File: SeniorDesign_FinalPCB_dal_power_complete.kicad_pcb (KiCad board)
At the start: 2 copper layers, 172.7 x 167.4 mm, 262 parts, among them J1 5000, J10 5000, J11 POWER, J12 AudioJack3, J2 5000, J3 5000, J4 5000, J5 5000, J6 5000, J7 5000, J8 5000, J9 5000, Q1 Si7450DP, Q10 Si7450DP, Q11 Si7450DP, Q12 Si7450DP, Q13 Si7450DP, Q14 Si7450DP, Q15 Si7450DP, Q16 Si7450DP, Q2 Si7450DP, Q3 Si7450DP, Q4 Si7450DP, Q5 Si7450DP, Q6 Si7450DP, Q7 Si7450DP, Q8 Si7450DP, Q9 Si7450DP, U1 Transducer, U10 Transducer, U11 Transducer, U12 Transducer, U13 Transducer, U14 Transducer, U15 Transducer, U16 Transducer, U17 Transducer, U18 Transducer, U19 Transducer, U2 Transducer, U20 Transducer, U21 Transducer, U22 Transducer, U23 Transducer, U24 Transducer, U25 Transducer, U26 Transducer, U27 Transducer, U28 Transducer, U29 Transducer, U3 Transducer, U30 Transducer, U31 Transducer, U32 Transducer, U33 Transducer, U34 Transducer, U35 Transducer, U36 Transducer, U37 Transducer, U38 Transducer, U39 Transducer, U4 Transducer, U40 Transducer, U41 Transducer, U42 Transducer, U43 Transducer, U44 Transducer, U45 Transducer, U46 Transducer, U47 Transducer, U48 Transducer, U49 Transducer, U5 Transducer, U50 Transducer, U51 Transducer, U52 Transducer, U53 Transducer, U54 Transducer, U55 Transducer, U56 Transducer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

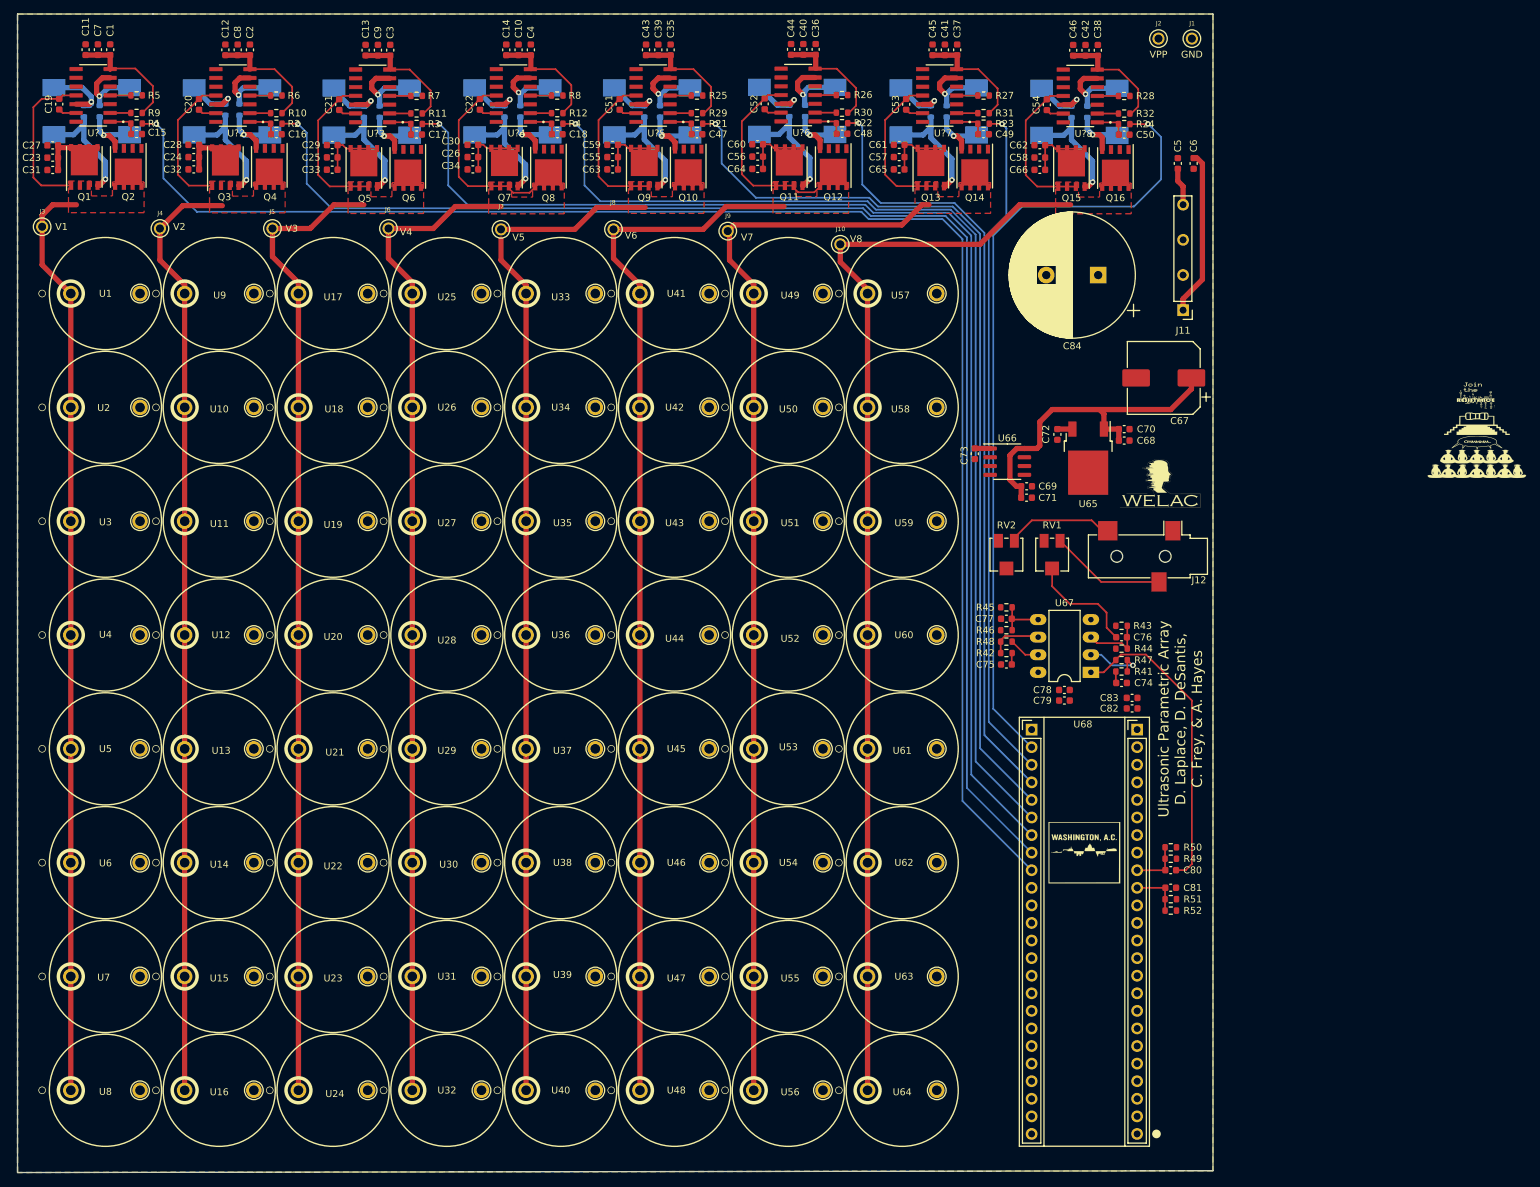
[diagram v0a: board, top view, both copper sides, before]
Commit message: Replaced 0603 Caps (VPP) with 1206
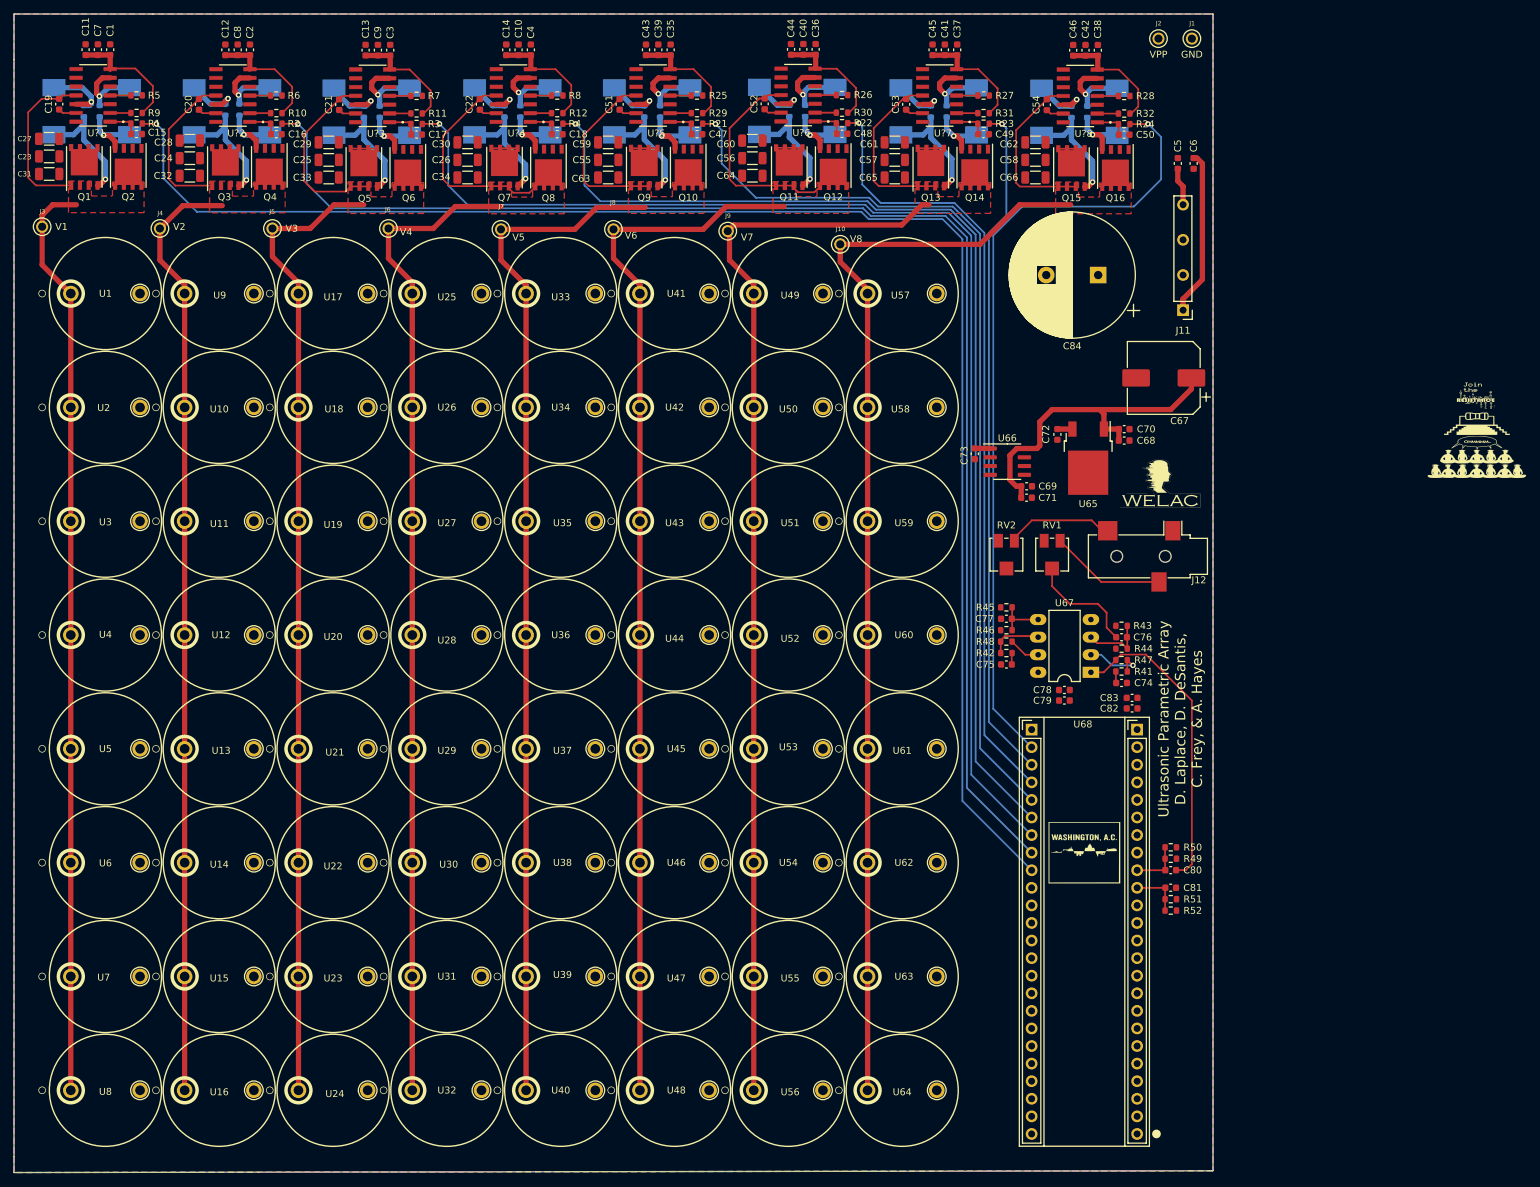
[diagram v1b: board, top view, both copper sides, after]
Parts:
- C23, C24, C25, C26, C27, C28, C29, C30, C31, C32, C33, C34, C55, C56, C57, C58, C59, C60, C61, C62, C63, C64, C65, C66: footprint Capacitor_SMD:C_0603_1608Metric -> SeniorDesign:C_1206_3216Metric
- moved C34 1.40 mm to (367.3, 43.4)
- moved C65 1.33 mm to (429.0, 43.4)
- moved C63 1.33 mm to (387.6, 43.4)
- moved C66 1.28 mm to (449.3, 43.4)
- moved C64 1.25 mm to (408.4, 43.2)
- moved C33 1.24 mm to (347.2, 43.4)
- moved C32 1.08 mm to (327.2, 43.2)
- moved C27 1.07 mm to (306.8, 37.8)
- moved C60 0.93 mm to (408.4, 38.1)
- moved C26 0.87 mm to (367.3, 40.9)
- moved C30 0.84 mm to (367.3, 38.4)
- moved C28 0.83 mm to (327.2, 38.1)
- moved C56 0.79 mm to (408.4, 40.6)
- moved C31 0.77 mm to (306.8, 42.9)
- moved C62 0.76 mm to (449.3, 38.4)
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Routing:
- net VPP: track 81.1 -> 28.4 mm
- net COL5_OUT: track 169.9 -> 174.8 mm
- net COL3_OUT: track 163.8 -> 167.8 mm
- net COL4_OUT: track 170.5 -> 174.0 mm
- net COL6_OUT: track 178.9 -> 182.3 mm
- net COL7_OUT: track 178.5 -> 181.6 mm
- net COL8_OUT: track 182.7 -> 185.3 mm
- net COL2_OUT: track 157.2 -> 159.4 mm
- net COL1_OUT: track 156.7 -> 157.8 mm
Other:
- board size 172.7 x 167.4 mm -> 173.2 x 167.4 mm

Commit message: Routing the rest of the things. (Subject to change)
This is my attempt at routing all of the rest of the things. I used (Pcbnew / Tools / Cleanup Tracks & Via’s) to remove all of the small "unconnected track" warnings we were getting and in this configuration I now get 14 errors, but the DRC completes.
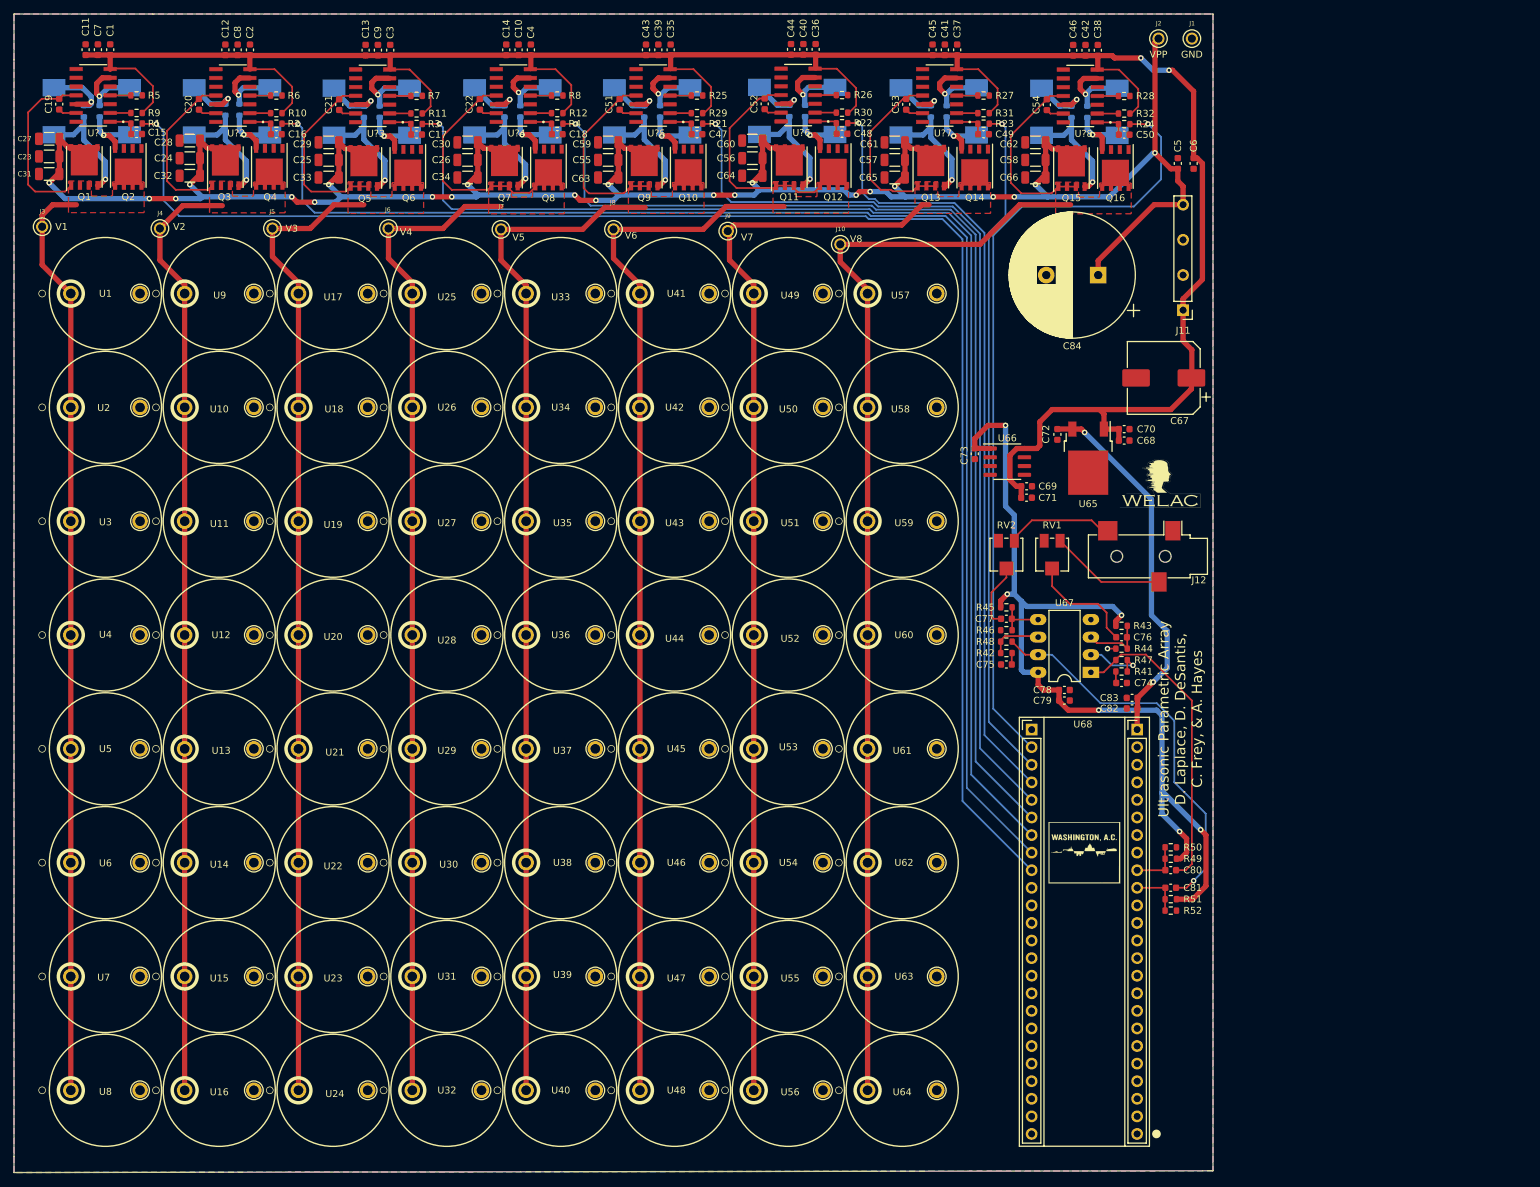
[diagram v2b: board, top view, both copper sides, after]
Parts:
- G*** (x2): moved to B.Cu
- moved G*** 62.2 mm to (452.2, 70.1), turned to 180 degrees
- moved G*** 56.2 mm to (455.2, 65.0), turned to 180 degrees
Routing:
- net VPP: track 28.4 -> 330.0 mm, vias 0 -> 23
- net +12V: track 207.6 -> 361.5 mm, vias 0 -> 2
- net +5VA: track 2.23 -> 135.1 mm, vias 0 -> 6
- net Net-(C81-Pad1): track 4.55 -> 56.8 mm, vias 0 -> 1
- net +5V: track 2.17 -> 53.8 mm, vias 0 -> 2
- net Net-(C77-Pad1): track 0.00 -> 9.40 mm
- net COL5_SIG: track 134.4 -> 136.8 mm
- net Net-(D2-Pad2): track 12.0 -> 9.71 mm
- net Net-(D5-Pad2): track 18.6 -> 16.7 mm
- net COL8_OUT: track 185.3 -> 187.2 mm
- net COL1_SIG: track 224.8 -> 226.6 mm
- net COL2_SIG: track 202.8 -> 204.6 mm
- net COL3_SIG: track 180.7 -> 182.4 mm
- net COL5_OUT: track 174.8 -> 176.2 mm
- net COL1_OUT: track 157.8 -> 159.1 mm
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
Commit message: final pre-design review push
Fixed some routing problems. Changed capacitor sizes for large bypass voltages. array modeled
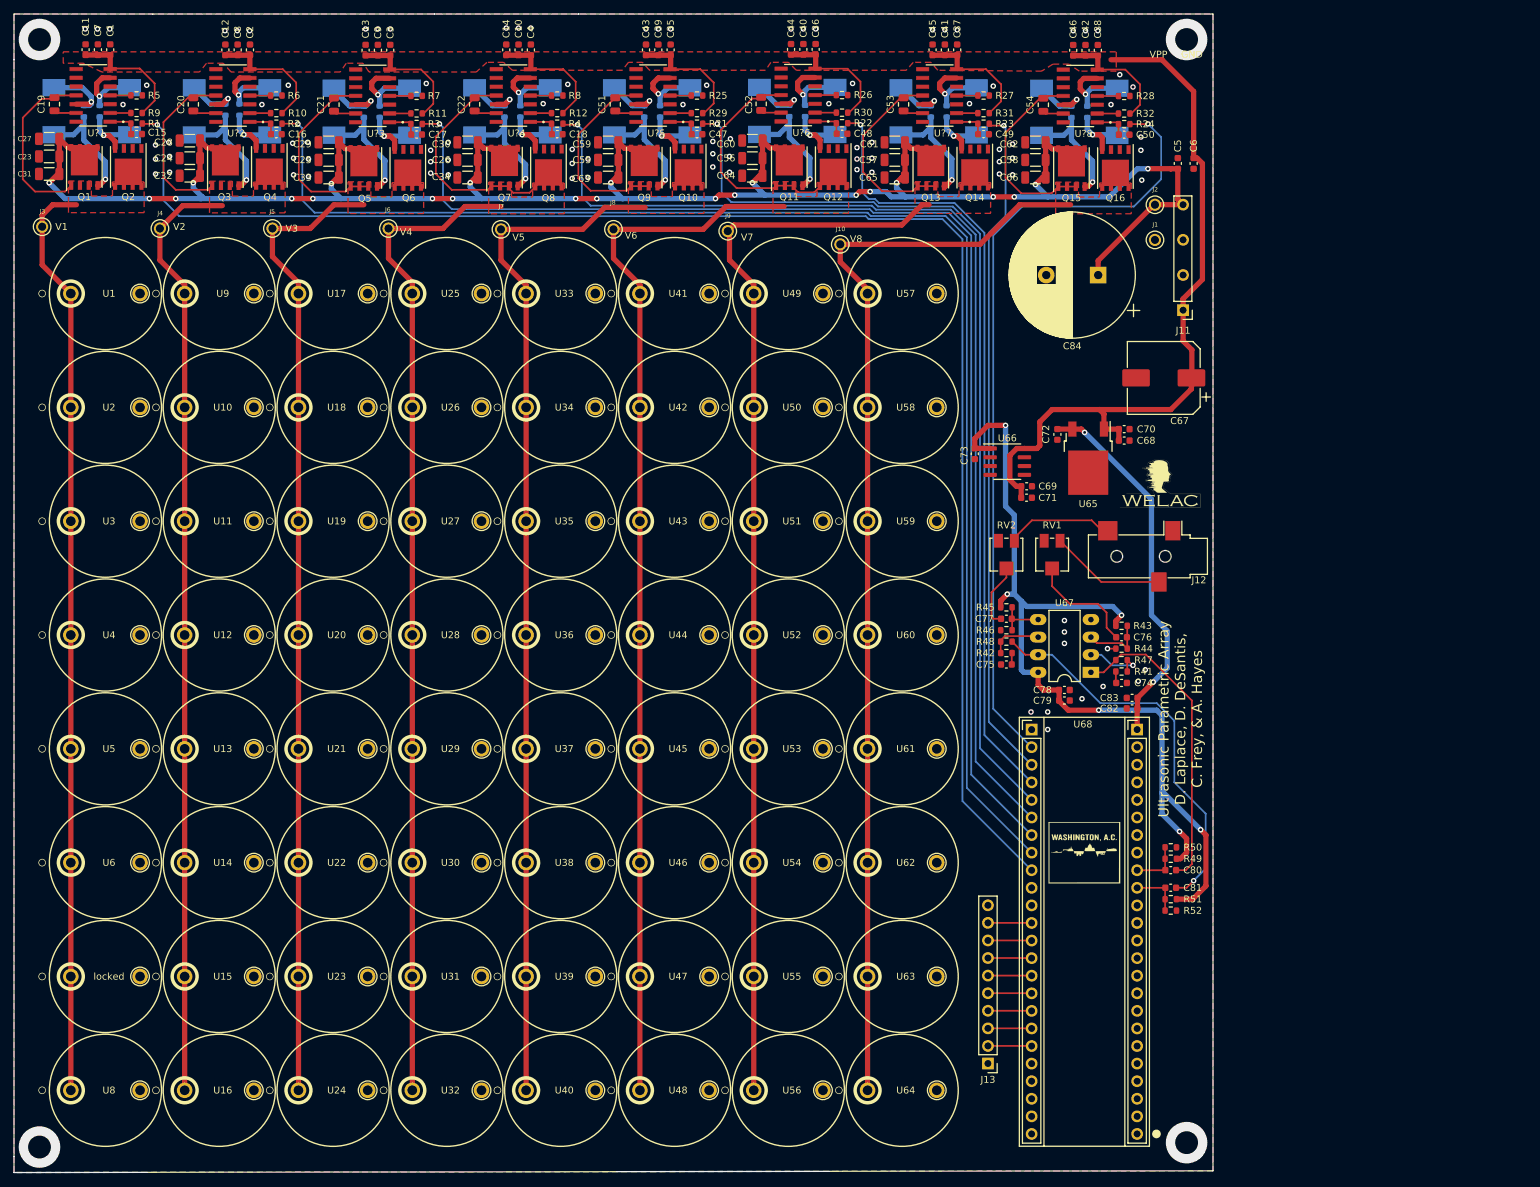
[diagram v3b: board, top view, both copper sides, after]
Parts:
- added J13: Conn_01x10_Male, Connector_PinHeader_2.54mm:PinHeader_1x10_P2.54mm_Vertical, F.Cu at (442.5, 171.4)
- C19, C20, C21, C22, C51, C52, C53, C54: value 0.1u -> 0.1u 100V; footprint Capacitor_SMD:C_0603_1608Metric -> Capacitor_SMD:C_0805_2012Metric
- C27, C29, C30, C59, C60, C61, C62: value 0.1u -> 0.1u 100V
- C28: value 1u -> 0.1u 100V
- C31, C32, C33, C34, C63, C64, C65, C66: value 0.1u -> 100p 100V
- U1, U10, U11, U12, U13, U14, U15, U16, U17, U18, U19, U2, U20, U21, U22, U23, U24, U25, U26, U27, U28, U29, U3, U30, U31, U32, U33, U34, U35, U36, U37, U38, U39, U4, U40, U41, U42, U43, U44, U45, U46, U47, U48, U49, U5, U50, U51, U52, U53, U54, U55, U56, U57, U58, U59, U6, U60, U61, U62, U63, U64, U8, U9: footprint SeniorDesign:Transducer -> Senior:Transducer
- locked: renamed from U7; footprint SeniorDesign:Transducer -> Senior:Transducer
- moved J1 29.6 mm to (466.6, 52.5)
- moved J2 24.0 mm to (466.6, 47.4)
- moved C20 0.82 mm to (327.7, 32.9)
- moved C21 0.76 mm to (348.0, 32.9)
- moved C22 0.76 mm to (368.3, 32.9)
- moved C19 0.69 mm to (307.6, 32.8)
- moved C51 0.63 mm to (388.6, 32.9)
- moved C52 0.51 mm to (409.7, 32.8)
- moved C54 0.51 mm to (450.5, 32.9)
- moved C53 0.38 mm to (430.3, 32.9)
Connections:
- U68 pad 36: unconnected-(U68-Pad36) -> Net-(J13-Pad9)
- U68 pad 37: unconnected-(U68-Pad37) -> Net-(J13-Pad8)
- U68 pad 38: unconnected-(U68-Pad38) -> Net-(J13-Pad7)
- U68 pad 39: unconnected-(U68-Pad39) -> Net-(J13-Pad6)
- U68 pad 40: unconnected-(U68-Pad40) -> Net-(J13-Pad5)
- U68 pad 41: unconnected-(U68-Pad41) -> Net-(J13-Pad4)
- U68 pad 42: unconnected-(U68-Pad42) -> Net-(J13-Pad3)
- U68 pad 43: unconnected-(U68-Pad43) -> Net-(J13-Pad2)
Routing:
- net +12V: track 361.5 -> 250.3 mm, vias 2 -> 0
- net VPP: track 330.0 -> 310.9 mm
- net Net-(J13-Pad8): track 0.00 -> 6.32 mm
- net Net-(J13-Pad5): track 0.00 -> 6.32 mm
- net Net-(J13-Pad4): track 0.00 -> 6.32 mm
- net Net-(J13-Pad9): track 0.00 -> 6.32 mm
- net Net-(J13-Pad7): track 0.00 -> 6.32 mm
- net Net-(J13-Pad6): track 0.00 -> 6.32 mm
- net Net-(J13-Pad3): track 0.00 -> 6.32 mm
- net Net-(J13-Pad2): track 0.00 -> 6.32 mm
- net COL6_OUT: track 182.7 -> 184.8 mm
- net COL8_OUT: track 187.2 -> 189.0 mm
- net COL2_OUT: track 160.5 -> 161.9 mm
- net COL7_OUT: track 182.8 -> 184.2 mm
- net COL3_OUT: track 168.1 -> 169.3 mm
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- added copper zone on F.Cu, net +12V
